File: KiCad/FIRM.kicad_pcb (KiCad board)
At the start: 4 copper layers, 40.5 x 40.5 mm, 98 parts, among them J2 DM3CS-SF, Q2 IRLML6402, U1 STM32F405RGTx, U2 MIC5219-3.3YM5, U6 A-USBC-20F0-EA-GSR05, U7 W25Q128JVS, X2 32.768khz, Y1 12 MHz

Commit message: oopsies
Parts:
- renumbered TP24 to C13
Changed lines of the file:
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@@
 		(descr "THT rectangular pad as test Point, square 1.5mm side length, hole diameter 0.7mm")
 		(tags "test point THT pad rectangle square")
-		(property "Reference" "TP24"
+		(property "Reference" "C13"
 			(at 0.01 -2.87 0)
 			(layer "B.SilkS")

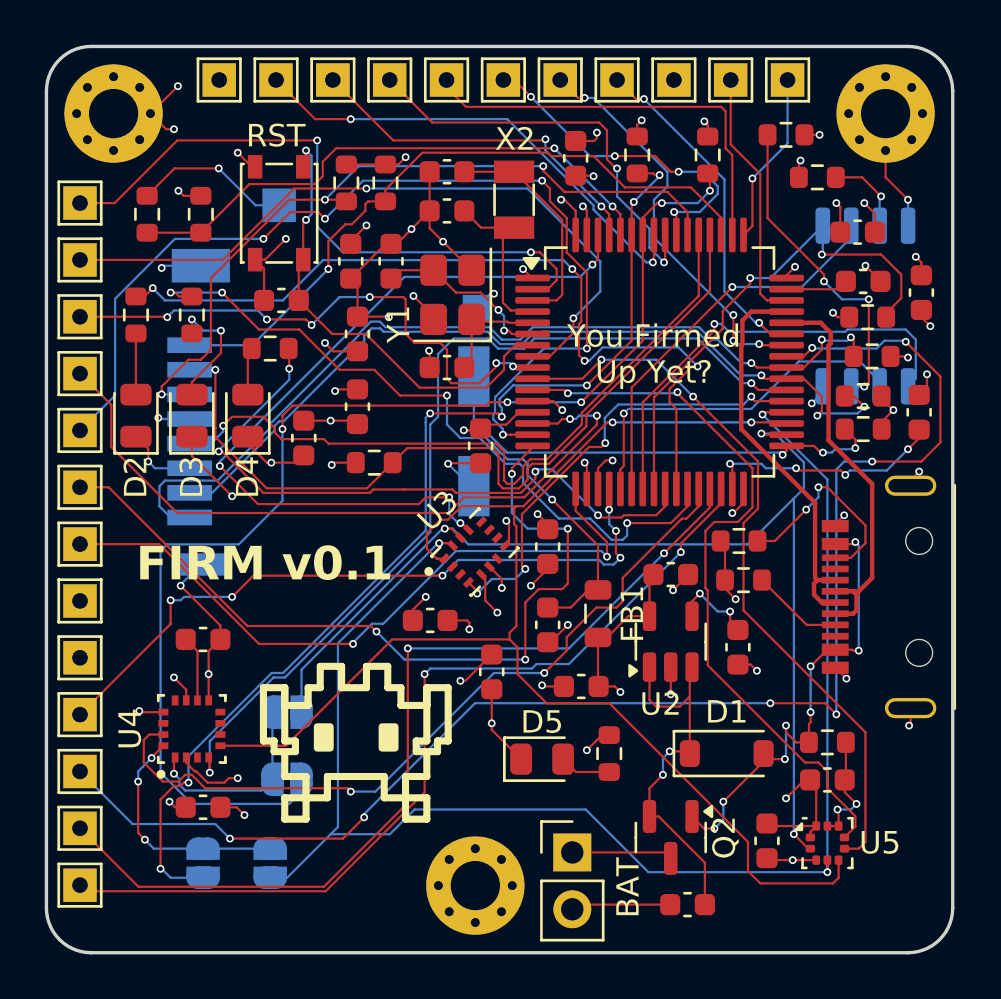
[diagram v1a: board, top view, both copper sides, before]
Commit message: Update via size
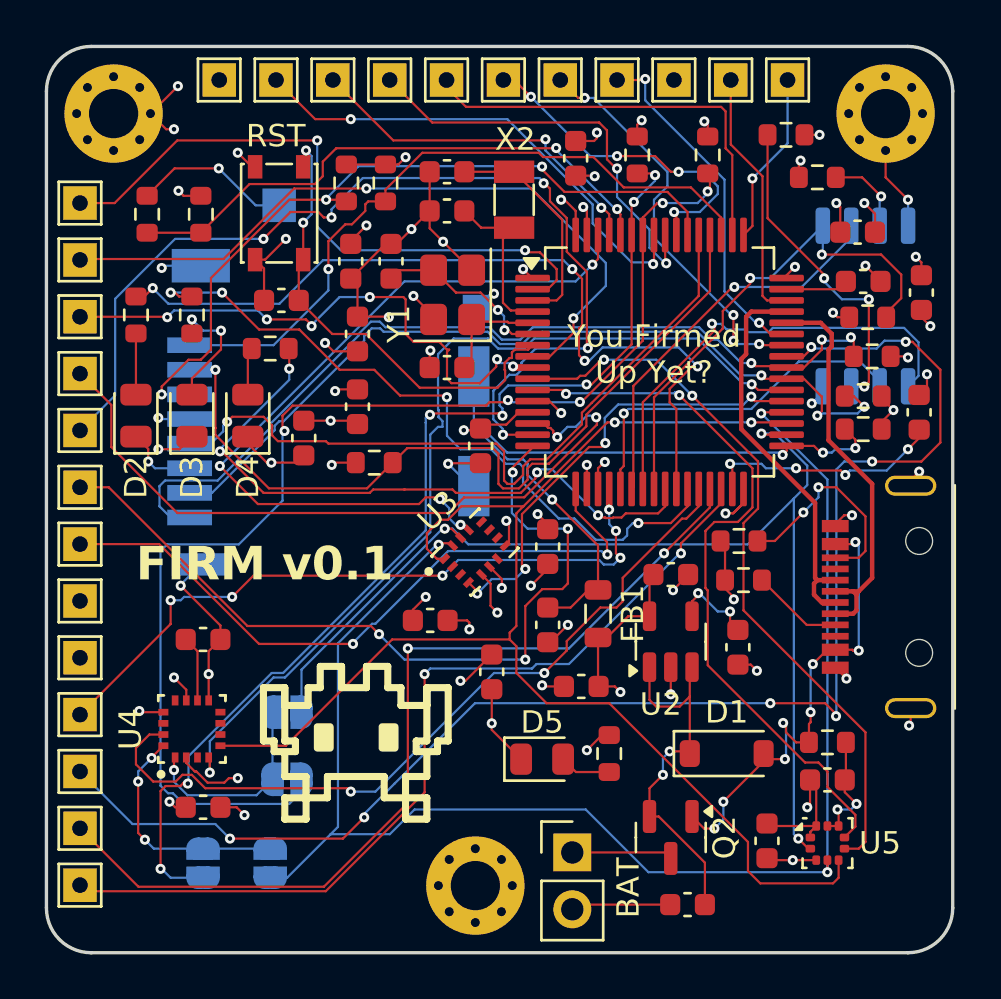
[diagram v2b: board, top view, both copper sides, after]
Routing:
- net GND: track 96.1 -> 94.6 mm
- net /PA1: track 44.6 -> 45.3 mm
- net /I2C1_SCL: track 55.0 -> 55.7 mm
- net /PC1: track 25.0 -> 25.6 mm
- net /PA10: track 15.2 -> 15.8 mm
- net /SDIO_D2: track 30.5 -> 31.1 mm
- net /PA0: track 31.8 -> 32.3 mm
